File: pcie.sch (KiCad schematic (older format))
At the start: 9 parts, among them P2 PCIE-064-02

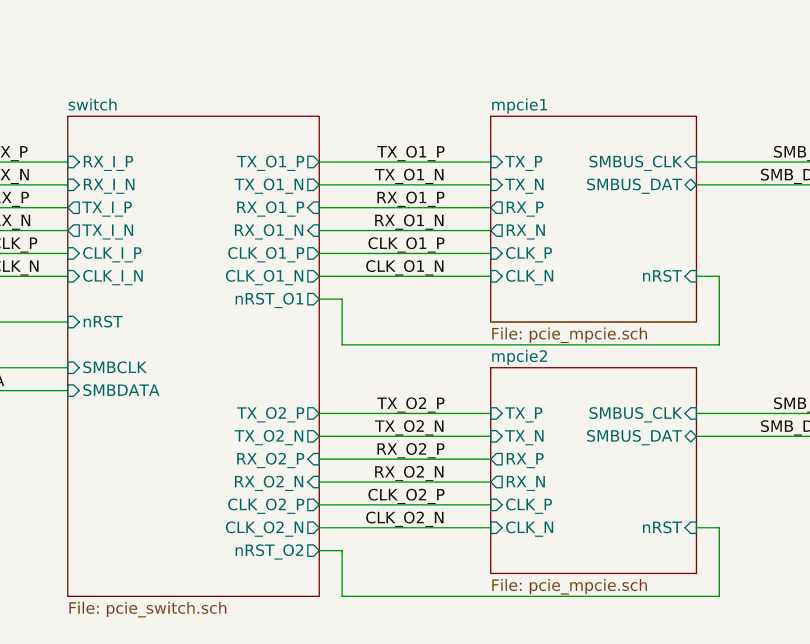
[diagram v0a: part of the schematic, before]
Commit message: sch: Swap some PCIe switch pairs for routing reasons
- Swap clock outputs
- Swap data polarities
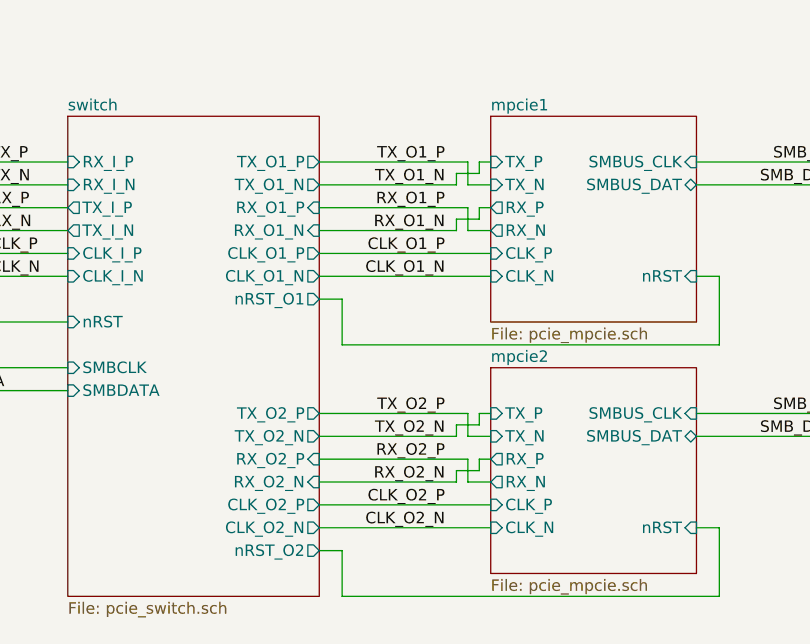
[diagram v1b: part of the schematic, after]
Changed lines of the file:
@@
 $EndSheet
 Wire Wire Line
-	3400 3300 4150 3300
-Wire Wire Line
-	3400 3400 4150 3400
-Wire Wire Line
-	3400 3500 4150 3500
-Wire Wire Line
-	3400 3600 4150 3600
+	3400 3400 4000 3400
+Wire Wire Line
+	3400 3600 4000 3600
 Wire Wire Line
 	3400 3700 4150 3700
@@
 	3400 3800 4150 3800
 Wire Wire Line
-	3400 4400 4150 4400
-Wire Wire Line
-	3400 4500 4150 4500
-Wire Wire Line
-	3400 4600 4150 4600
-Wire Wire Line
-	3400 4700 4150 4700
+	3400 4500 4000 4500
+Wire Wire Line
+	3400 4700 4000 4700
 Wire Wire Line
 	3400 4800 4150 4800
@@
 Text Label 2200 1300 2    50   ~ 0
 SMB_DATA
-Text Label 3950 3500 2    50   ~ 0
-RX_O1_P
 Text Label 3950 3600 2    50   ~ 0
 RX_O1_N
-Text Label 3950 3300 2    50   ~ 0
-TX_O1_P
-Text Label 3950 3400 2    50   ~ 0
-TX_O1_N
 Text Label 3950 3700 2    50   ~ 0
 CLK_O1_P
@@
 Text Label 3950 4900 2    50   ~ 0
 CLK_O2_N
+Text Label 3950 3500 2    50   ~ 0
+RX_O1_P
+Text Label 3950 3400 2    50   ~ 0
+TX_O1_N
+Text Label 3950 3300 2    50   ~ 0
+TX_O1_P
+Wire Wire Line
+	4050 3300 4050 3400
+Wire Wire Line
+	4050 3400 4150 3400
+Wire Wire Line
+	3400 3300 4050 3300
+Wire Wire Line
+	4000 3400 4000 3350
+Wire Wire Line
+	4000 3350 4100 3350
+Wire Wire Line
+	4100 3350 4100 3300
+Wire Wire Line
+	4100 3300 4150 3300
+Wire Wire Line
+	4050 3500 4050 3600
+Wire Wire Line
+	4050 3600 4150 3600
+Wire Wire Line
+	3400 3500 4050 3500
+Wire Wire Line
+	4050 4400 4050 4500
+Wire Wire Line
+	4050 4500 4150 4500
+Wire Wire Line
+	3400 4400 4050 4400
+Wire Wire Line
+	4050 4600 4050 4700
+Wire Wire Line
+	4050 4700 4150 4700
+Wire Wire Line
+	3400 4600 4050 4600
+Wire Wire Line
+	4000 4700 4000 4650
+Wire Wire Line
+	4000 4650 4100 4650
+Wire Wire Line
+	4100 4650 4100 4600
+Wire Wire Line
+	4100 4600 4150 4600
+Wire Wire Line
+	4000 3600 4000 3550
+Wire Wire Line
+	4000 3550 4100 3550
+Wire Wire Line
+	4100 3550 4100 3500
+Wire Wire Line
+	4100 3500 4150 3500
+Wire Wire Line
+	4000 4500 4000 4450
+Wire Wire Line
+	4000 4450 4100 4450
+Wire Wire Line
+	4100 4450 4100 4400
+Wire Wire Line
+	4100 4400 4150 4400
 $EndSCHEMATC

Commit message: sch, pcb: Add testpads on lots of signals
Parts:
- added TP11, TP12: TestPoint, TestPoint:TestPoint_Pad_D1.0mm, symbol Connector:TestPoint
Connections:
- net mpcie1/nRST: now also TP11.1
- net mpcie2/nRST: now also TP12.1
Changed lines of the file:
@@
 Wire Wire Line
 	4100 4400 4150 4400
+$Comp
+L Connector:TestPoint TP?
+U 1 1 5D34022F
+P 5250 3800
+AR Path="/5D05A5E1/5D34022F" Ref="TP?"  Part="1"
+AR Path="/5CE77C37/5D34022F" Ref="TP?"  Part="1"
+AR Path="/5C91A44F/5D34022F" Ref="TP11"  Part="1"
+F 0 "TP11" V 5250 3988 50  0000 L CNN
+F 1 "TestPoint" V 5295 3988 50  0001 L CNN
+F 2 "TestPoint:TestPoint_Pad_D1.0mm" H 5450 3800 50  0001 C CNN
+F 3 "~" H 5450 3800 50  0001 C CNN
+	1    5250 3800
+	0    1    1    0
+$EndComp
+$Comp
+L Connector:TestPoint TP?
+U 1 1 5D348793
+P 5250 4900
+AR Path="/5D05A5E1/5D348793" Ref="TP?"  Part="1"
+AR Path="/5CE77C37/5D348793" Ref="TP?"  Part="1"
+AR Path="/5C91A44F/5D348793" Ref="TP12"  Part="1"
+F 0 "TP12" V 5250 5088 50  0000 L CNN
+F 1 "TestPoint" V 5295 5088 50  0001 L CNN
+F 2 "TestPoint:TestPoint_Pad_D1.0mm" H 5450 4900 50  0001 C CNN
+F 3 "~" H 5450 4900 50  0001 C CNN
+	1    5250 4900
+	0    1    1    0
+$EndComp
+Wire Wire Line
+	5150 3800 5250 3800
+Connection ~ 5150 3800
+Wire Wire Line
+	5150 4900 5250 4900
+Connection ~ 5150 4900
 $EndSCHEMATC
